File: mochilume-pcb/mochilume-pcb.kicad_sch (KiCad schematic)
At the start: 17 parts

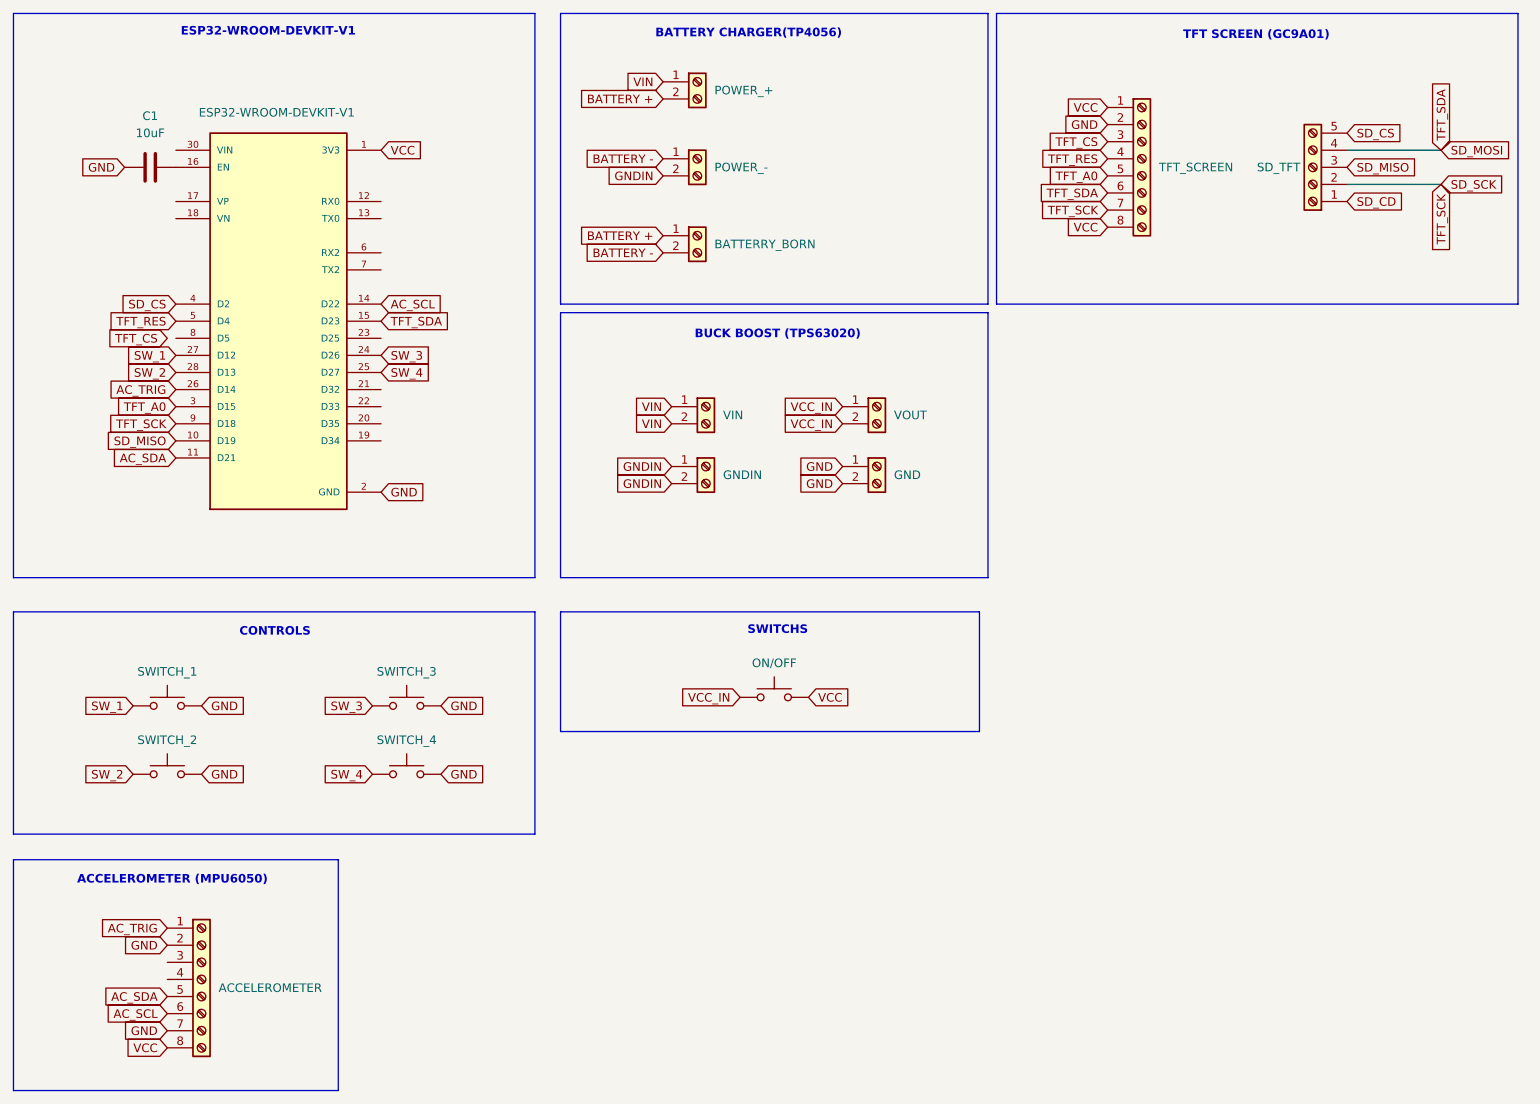
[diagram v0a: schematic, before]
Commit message: feat: assign footprints and trails to plate
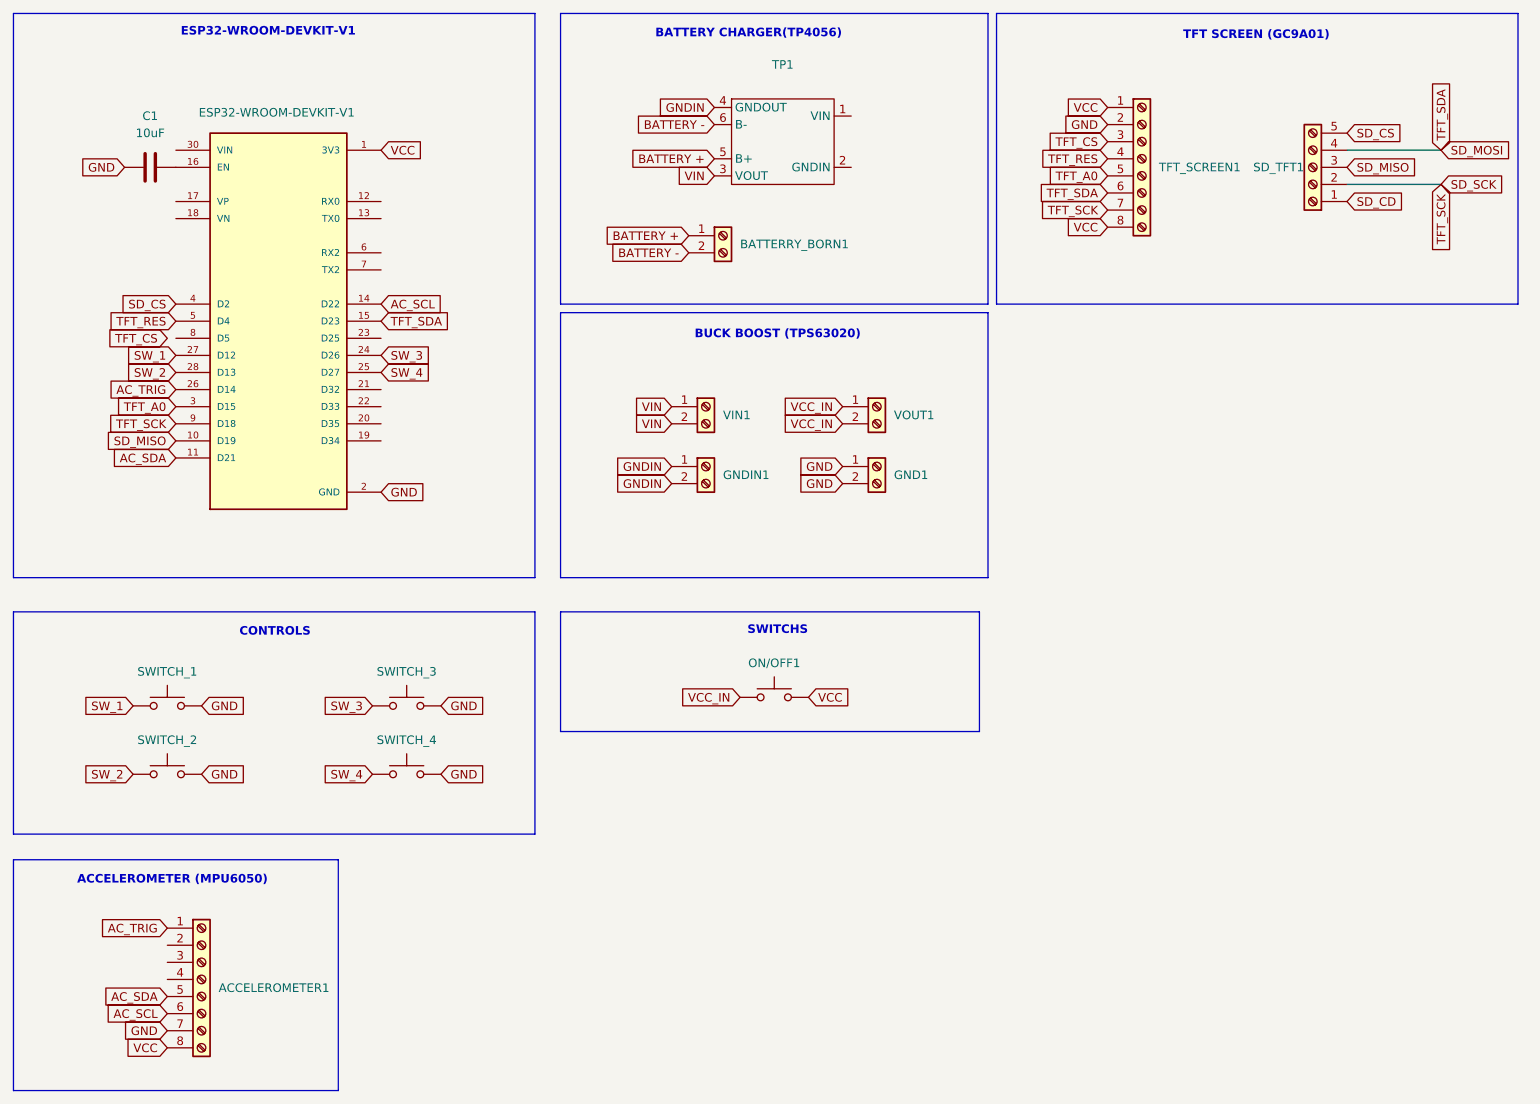
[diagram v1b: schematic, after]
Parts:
- removed POWER_+, POWER_-: Screw_Terminal_01x02, symbol Connector:Screw_Terminal_01x02
- added TP1: ~, Library:TP4056-18650, symbol teste_lib_kicad:TP4056
- ACCELEROMETER1: renamed from ACCELEROMETER; value ACELERÔMETRO -> ~; footprint (none) -> Connector_PinHeader_2.54mm:PinHeader_1x08_P2.54mm_Vertical
- BATTERRY_BORN1: renamed from BATTERRY_BORN; value Screw_Terminal_01x02 -> ~; footprint (none) -> TerminalBlock_Phoenix:TerminalBlock_Phoenix_MKDS-1,5-2-5.08_1x02_P5.08mm_Horizontal
- C1: footprint (none) -> Capacitor_THT:CP_Radial_D4.0mm_P2.00mm
- ESP32-WROOM-DEVKIT-V1: value ESP32-DEVKIT-V1 -> ~; footprint ESP32-DEVKIT-V1:MODULE_ESP32_DEVKIT_V1 -> Library:MODULE_ESP32_DEVKIT_V1
- GND1: renamed from GND; value Screw_Terminal_01x02 -> ~; footprint (none) -> Connector_PinHeader_2.54mm:PinHeader_1x02_P2.54mm_Vertical
- GNDIN1: renamed from GNDIN; value Screw_Terminal_01x02 -> ~; footprint (none) -> Connector_PinHeader_2.54mm:PinHeader_1x02_P2.54mm_Vertical
- ON/OFF1: renamed from ON/OFF; value BOTÃO_3 -> ~; footprint (none) -> TerminalBlock_Phoenix:TerminalBlock_Phoenix_MKDS-1,5-2-5.08_1x02_P5.08mm_Horizontal
- SD_TFT1: renamed from SD_TFT; value Screw_Terminal_01x05 -> ~; footprint (none) -> Connector_PinHeader_2.54mm:PinHeader_1x05_P2.54mm_Vertical
- SWITCH_1: value BOTÃO_1 -> ~; footprint (none) -> Button_Switch_THT:SW_PUSH_6mm
- SWITCH_2: value BOTÃO_2 -> ~; footprint (none) -> Button_Switch_THT:SW_PUSH_6mm
- SWITCH_3: value BOTÃO_3 -> ~; footprint (none) -> Button_Switch_THT:SW_PUSH_6mm
- SWITCH_4: value BOTÃO_4 -> ~; footprint (none) -> Button_Switch_THT:SW_PUSH_6mm
- TFT_SCREEN1: renamed from TFT_SCREEN; value ACELERÔMETRO -> ~; footprint (none) -> Connector_PinHeader_2.54mm:PinHeader_1x08_P2.54mm_Vertical
- VIN1: renamed from VIN; value Screw_Terminal_01x02 -> ~; footprint (none) -> Connector_PinHeader_2.54mm:PinHeader_1x02_P2.54mm_Vertical
- VOUT1: renamed from VOUT; value Screw_Terminal_01x02 -> ~; footprint (none) -> Connector_PinHeader_2.54mm:PinHeader_1x02_P2.54mm_Vertical
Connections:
- net BATTERY +: now also TP1.5 (B+)
- net BATTERY -: now also TP1.6 (B-)
- net GND: no longer ACCELEROMETER1.2 (Pin_2)
- net GNDIN: now also TP1.4 (GNDOUT)
- net VIN: now also TP1.3 (VOUT)
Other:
- moved on the sheet: BATTERRY_BORN1
